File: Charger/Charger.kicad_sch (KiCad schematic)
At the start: 2 parts, among them J1 Charger output, SW1 Charger_Switch

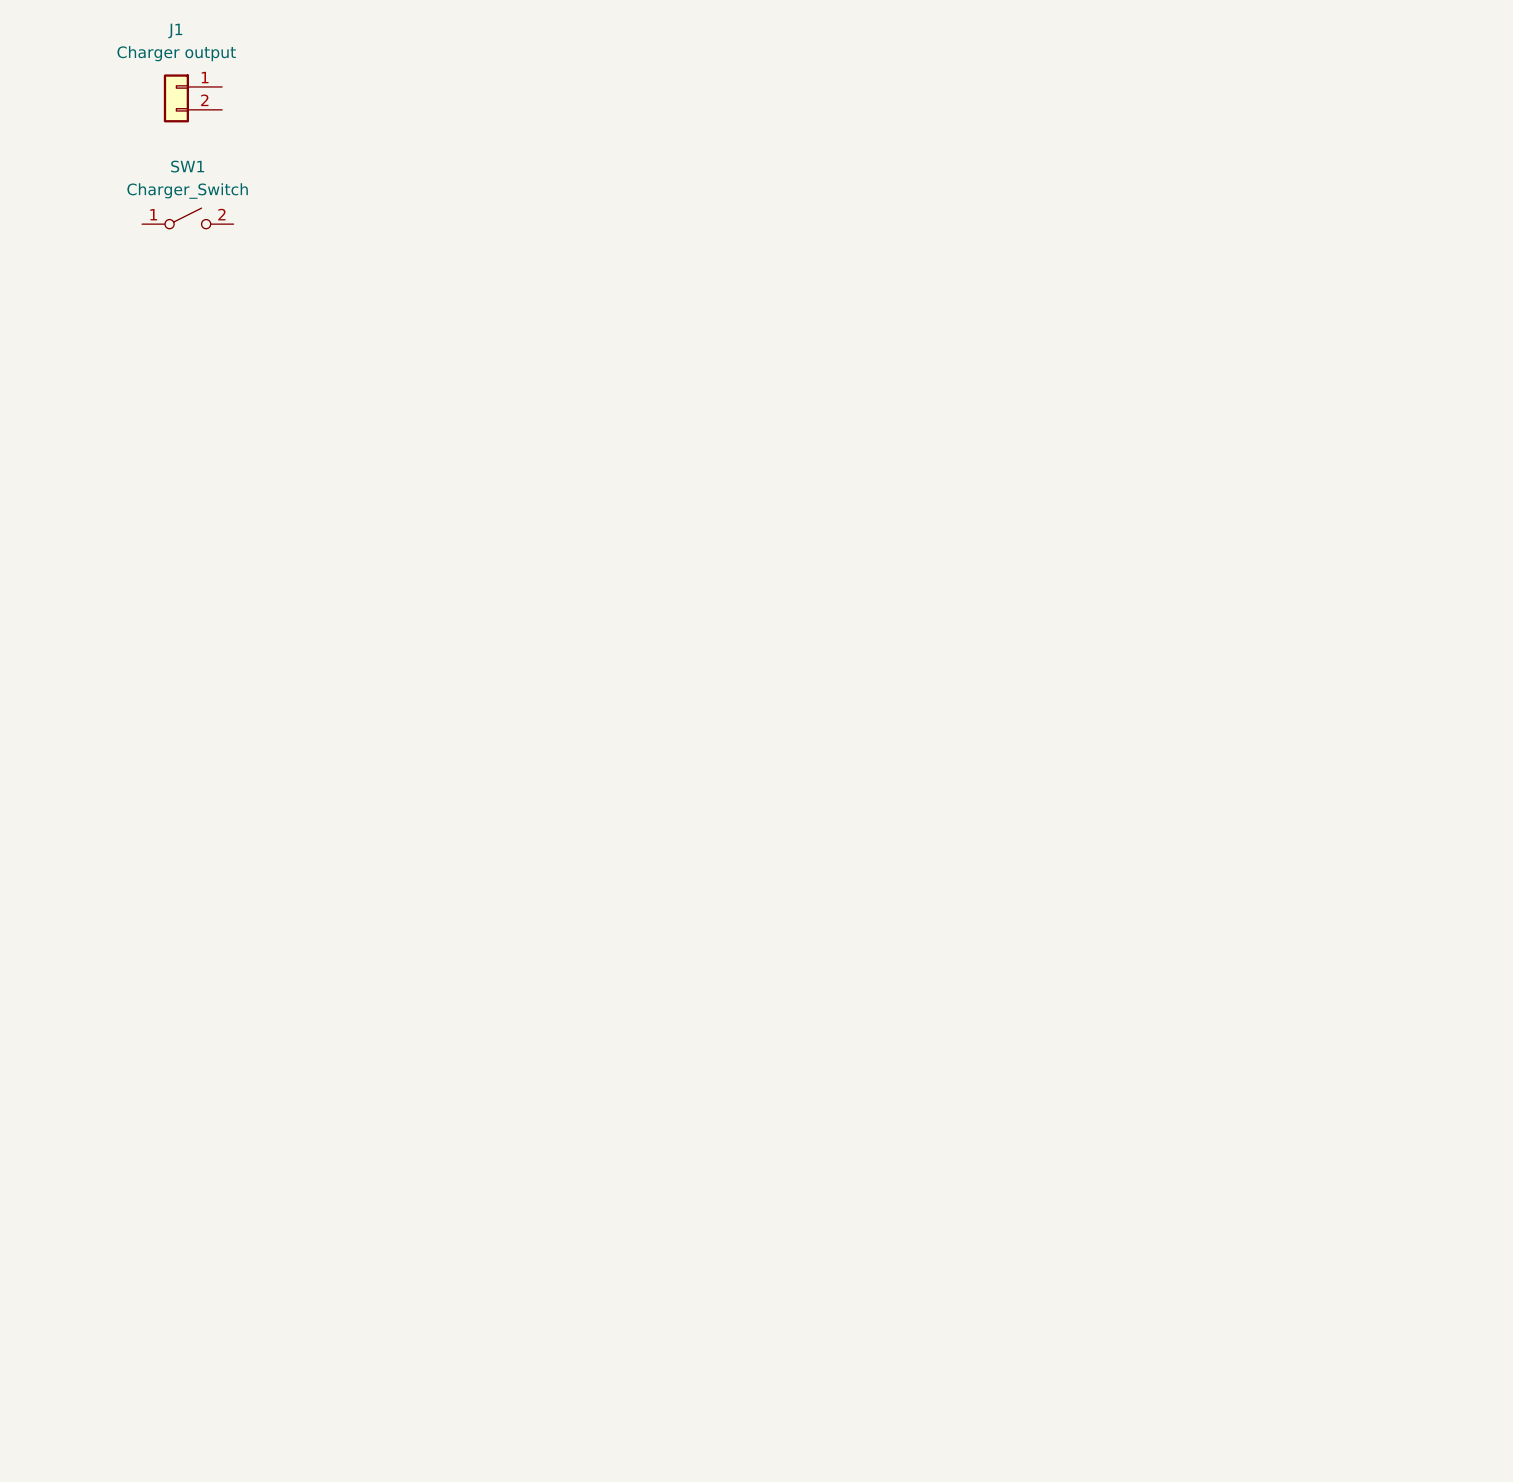
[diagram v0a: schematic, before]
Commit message: dot car charger
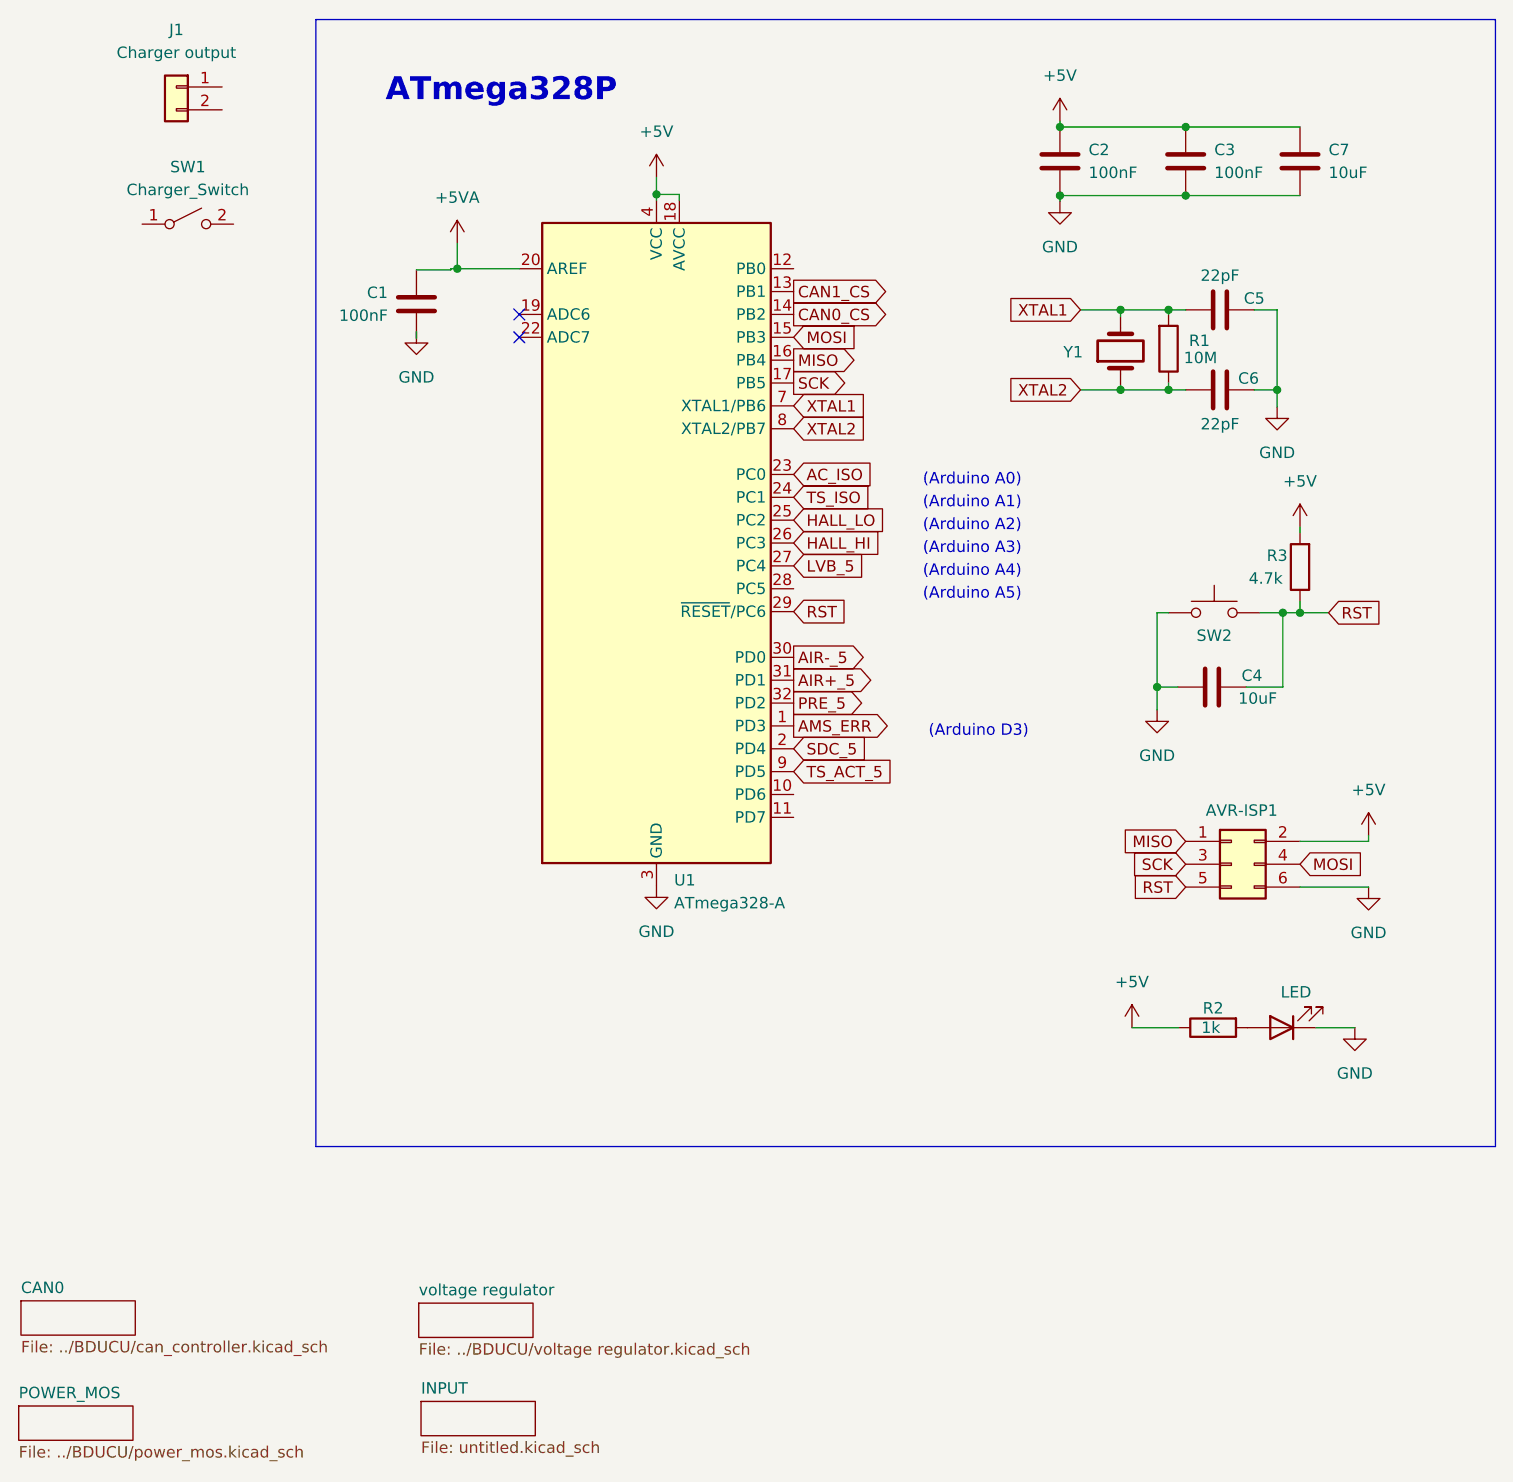
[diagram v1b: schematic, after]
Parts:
- added AVR-ISP1: Conn_02x03_Odd_Even, Connector_PinHeader_2.54mm:PinHeader_2x03_P2.54mm_Vertical, symbol Connector_Generic:Conn_02x03_Odd_Even
- added C1, C2, C3: 100nF, RMC_Capacitor:C_0805_2012Metric_Pad1.18x1.45mm_HandSolder_L, symbol Device:C
- added C4, C7: 10uF, RMC_Capacitor:C_0805_2012Metric_Pad1.18x1.45mm_HandSolder_L, symbol Device:C
- added C5, C6: 22pF, RMC_Capacitor:C_0805_2012Metric_Pad1.18x1.45mm_HandSolder_L, symbol Device:C
- added D1: LED, RMC_LED:LED_0805_2012Metric_Pad1.45x1.40mm_HandSolder, symbol Device:LED
- added R1: 10M, RMC_Resistor:R_0805_2012Metric_Pad1.20x1.40mm_HandSolder_L, symbol Device:R
- added R2: 1k, RMC_Resistor:R_0805_2012Metric_Pad1.20x1.40mm_HandSolder_L, symbol Device:R
- added R3: 4.7k, RMC_Resistor:R_0805_2012Metric_Pad1.20x1.40mm_HandSolder_L, symbol Device:R
- added SW2: SW_Push, Button_Switch_SMD:SW_SPST_CK_RS282G05A3, symbol Switch:SW_Push
- added U1: ATmega328-A, RMC_QFP:TQFP-32_7x7mm_P0.8mm_L, symbol MCU_Microchip_ATmega:ATmega328-A
- added Y1: 20MHz, RMC_Crystal:Crystal_HC49-U_Vertical_W_SMD, symbol Device:Crystal
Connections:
- new net: D1.2 (A), R2.2
- new net +5V: AVR-ISP1.2 (Pin_2), C2.2, C3.2, C7.2, R2.1, R3.2, U1.18 (AVCC), U1.4 (VCC), U1.6 (VCC)
- new net +5VA: C1.2, U1.20 (AREF)
- new net AC_ISO: U1.23 (PC0)
- new net AIR+_5: U1.31 (PD1)
- new net AIR-_5: U1.30 (PD0)
- new net AMS_ERR: U1.1 (PD3)
- new net CAN0_CS: U1.14 (PB2)
- new net CAN1_CS: U1.13 (PB1)
- new net GND: AVR-ISP1.6 (Pin_6), C1.1, C2.1, C3.1, C4.1, C5.1, C6.1, C7.1, D1.1 (K), SW2.1, U1.21 (GND), U1.3 (GND), U1.5 (GND)
- new net HALL_HI: U1.26 (PC3)
- new net HALL_LO: U1.25 (PC2)
- new net LVB_5: U1.27 (PC4)
- new net MISO: AVR-ISP1.1 (Pin_1), U1.16 (PB4)
- new net MOSI: AVR-ISP1.4 (Pin_4), U1.15 (PB3)
- new net PRE_5: U1.32 (PD2)
- new net RST: AVR-ISP1.5 (Pin_5), C4.2, R3.1, SW2.2, U1.29 (~{RESET}/PC6)
- new net SCK: AVR-ISP1.3 (Pin_3), U1.17 (PB5)
- new net SDC_5: U1.2 (PD4)
- new net TS_ACT_5: U1.9 (PD5)
- new net TS_ISO: U1.24 (PC1)
- new net XTAL1: C5.2, R1.2, U1.7 (XTAL1/PB6), Y1.2
- new net XTAL2: C6.2, R1.1, U1.8 (XTAL2/PB7), Y1.1
- no-connect marks 0 -> 2
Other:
- added sheet CAN0 (../BDUCU/can_controller.kicad_sch)
- added sheet INPUT (untitled.kicad_sch)
- added sheet POWER_MOS (../BDUCU/power_mos.kicad_sch)
- added sheet voltage regulator (../BDUCU/voltage regulator.kicad_sch)
- note added: "(Arduino A0)"
- note added: "(Arduino A1)"
- note added: "(Arduino A2)"
- note added: "(Arduino A3)"
- note added: "(Arduino A4)"
- note added: "(Arduino A5)"
- note added: "(Arduino D3)"
- note added: "ATmega328P"

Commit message: CHARGER
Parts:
- removed J1: Charger output, symbol Connector_Generic:Conn_01x02
- removed SW1: Charger_Switch, symbol Switch:SW_SPST
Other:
- added sheet Connectors (connectors.kicad_sch)
- added sheet DIGIPOT (DIGIPOT.kicad_sch)
- sheet CAN0 ports: added CAN_H, CAN_L, CS, MISO, MOSI, SCK; removed none
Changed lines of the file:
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@@
-	)
-	(symbol
-		(lib_id "Connector_Generic:Conn_01x02")
-		(at 38.1 38.1 0)
-		(mirror y)
-		(unit 1)
-		(exclude_from_sim no)
-		(in_bom yes)
-		(on_board yes)
-		(dnp no)
-		(fields_autoplaced yes)
-		(property "Reference" "J1"
-			(at 38.1 31.75 0)
-			(effects
-				(font
-					(size 1.27 1.27)
-				)
-			)
-		)
-		(property "Value" "Charger output"
-			(at 38.1 34.29 0)
-			(effects
-				(font
-					(size 1.27 1.27)
-				)
-			)
-		)
-		(property "Footprint" ""
-			(at 38.1 38.1 0)
-			(effects
-				(font
-					(size 1.27 1.27)
-				)
-				(hide yes)
-			)
-		)
-		(property "Datasheet" "~"
-			(at 38.1 38.1 0)
-			(effects
-				(font
-					(size 1.27 1.27)
-				)
-				(hide yes)
-			)
-		)
-		(property "Description" "Generic connector, single row, 01x02, script generated (kicad-library-utils/schlib/autogen/connector/)"
-			(at 38.1 38.1 0)
-			(effects
-				(font
-					(size 1.27 1.27)
-				)
-				(hide yes)
-			)
-		)
-		(pin "2"
-		)
-		(pin "1"
-		)
-		(instances
-			(project ""
-				(path "/ba218c5d-b6ee-4635-9cf5-de406e83bbdf"
-					(reference "J1")
-					(unit 1)
-				)
-			)
-		)
 	)
 	(symbol
@@
 	)
 	(symbol
-		(lib_id "Switch:SW_SPST")
-		(at 39.37 53.34 0)
-		(unit 1)
-		(exclude_from_sim no)
-		(in_bom yes)
-		(on_board yes)
-		(dnp no)
-		(fields_autoplaced yes)
-		(property "Reference" "SW1"
-			(at 39.37 46.99 0)
-			(effects
-				(font
-					(size 1.27 1.27)
-				)
-			)
-		)
-		(property "Value" "Charger_Switch"
-			(at 39.37 49.53 0)
-			(effects
-				(font
-					(size 1.27 1.27)
-				)
-			)
-		)
-		(property "Footprint" ""
-			(at 39.37 53.34 0)
-			(effects
-				(font
-					(size 1.27 1.27)
-				)
-				(hide yes)
-			)
-		)
-		(property "Datasheet" "~"
-			(at 39.37 53.34 0)
-			(effects
-				(font
-					(size 1.27 1.27)
-				)
-				(hide yes)
-			)
-		)
-		(property "Description" "Single Pole Single Throw (SPST) switch"
-			(at 39.37 53.34 0)
-			(effects
-				(font
-					(size 1.27 1.27)
-				)
-				(hide yes)
-			)
-		)
-		(pin "2"
-		)
-		(pin "1"
-		)
-		(instances
-			(project ""
-				(path "/ba218c5d-b6ee-4635-9cf5-de406e83bbdf"
-					(reference "SW1")
-					(unit 1)
-				)
-			)
-		)
-	)
-	(symbol
 		(lib_id "Device:R")
 		(at 162.941 91.44 180)
@@
 	)
 	(sheet
-		(at 65.278 184.15)
+		(at 20.955 156.845)
 		(size 12.7 3.81)
 		(exclude_from_sim no)
@@
 			(color 0 0 0 0.0000)
 		)
+		(property "Sheetname" "Connectors"
+			(at 20.955 156.1334 0)
+			(effects
+				(font
+					(size 1.27 1.27)
+				)
+				(justify left bottom)
+			)
+		)
+		(property "Sheetfile" "connectors.kicad_sch"
+			(at 20.955 161.2396 0)
+			(effects
+				(font
+					(size 1.27 1.27)
+				)
+				(justify left top)
+			)
+		)
+		(property "Field2" ""
+			(at 20.955 156.845 0)
+			(effects
+				(font
+					(size 1.27 1.27)
+				)
+			)
+		)
+		(instances
+			(project "Charger"
+				(path "/ba218c5d-b6ee-4635-9cf5-de406e83bbdf"
+					(page "6")
+				)
+			)
+		)
+	)
+	(sheet
+		(at 65.278 184.15)
+		(size 12.7 3.81)
+		(exclude_from_sim no)
+		(in_bom yes)
+		(on_board yes)
+		(dnp no)
+		(fields_autoplaced yes)
+		(stroke
+			(width 0.1524)
+			(type solid)
+		)
+		(fill
+			(color 0 0 0 0.0000)
+		)
 		(property "Sheetname" "INPUT"
 			(at 65.278 183.4384 0)
@@
 	)
 	(sheet
-		(at 20.828 172.974)
+		(at 113.03 173.99)
 		(size 12.7 3.81)
 		(exclude_from_sim no)
@@
 			(color 0 0 0 0.0000)
 		)
+		(property "Sheetname" "DIGIPOT"
+			(at 113.03 173.2784 0)
+			(effects
+				(font
+					(size 1.27 1.27)
+				)
+				(justify left bottom)
+			)
+		)
+		(property "Sheetfile" "DIGIPOT.kicad_sch"
+			(at 113.03 178.3846 0)
+			(effects
+				(font
+					(size 1.27 1.27)
+				)
+				(justify left top)
+			)
+		)
+		(instances
+			(project "Charger"
+				(path "/ba218c5d-b6ee-4635-9cf5-de406e83bbdf"
+					(page "7")
+				)
+			)
+		)
+	)
+	(sheet
+		(at 20.828 166.624)
+		(size 14.097 11.811)
+		(exclude_from_sim no)
+		(in_bom yes)
+		(on_board yes)
+		(dnp no)
+		(fields_autoplaced yes)
+		(stroke
+			(width 0.1524)
+			(type solid)
+		)
+		(fill
+			(color 0 0 0 0.0000)
+		)
 		(property "Sheetname" "CAN0"
-			(at 20.828 172.2624 0)
+			(at 20.828 165.9124 0)
 			(effects
 				(font
@@
 		)
 		(property "Sheetfile" "../BDUCU/can_controller.kicad_sch"
-			(at 20.828 177.3686 0)
+			(at 20.828 179.0196 0)
 			(effects
 				(font
@@
 			)
 		)
+		(pin "CAN_H" input
+			(at 34.925 171.45 0)
+			(effects
+				(font
+					(size 1.27 1.27)
+				)
+				(justify right)
+			)
+		)
+		(pin "CS" input
+			(at 20.828 176.53 180)
+			(effects
+				(font
+					(size 1.27 1.27)
+				)
+				(justify left)
+			)
+		)
+		(pin "MISO" input
+			(at 20.828 168.91 180)
+			(effects
+				(font
+					(size 1.27 1.27)
+				)
+				(justify left)
+			)
+		)
+		(pin "MOSI" input
+			(at 20.828 171.45 180)
+			(effects
+				(font
+					(size 1.27 1.27)
+				)
+				(justify left)
+			)
+		)
+		(pin "SCK" input
+			(at 20.828 173.99 180)
+			(effects
+				(font
+					(size 1.27 1.27)
+				)
+				(justify left)
+			)
+		)
+		(pin "CAN_L" input
+			(at 34.925 173.99 0)
+			(effects
+				(font
+					(size 1.27 1.27)
+				)
+				(justify right)
+			)
+		)

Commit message: funny stuffs
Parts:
- added J1: PL00X-301-10M8, symbol Connector_Generic:Conn_01x03
- added J2: PL00Y-301-10M8, symbol Connector_Generic:Conn_01x03
- added K1: Gigavc PNC11BDA, symbol Relay:Relay_SPST-NC
- added R4: discharge resistor, symbol Device:R
- added SW1: Emergency Button, symbol Switch:SW_Push
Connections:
- net AMS_ERR: no longer U1.1 (PD3)
- net GND: now also K1.A1
- net AC_ISO: no longer names the net of U1.23 (PC0)
- net AIR+_5: no longer names the net of U1.31 (PD1)
- net AIR-_5: no longer names the net of U1.30 (PD0)
- net CAN1_CS: no longer names the net of U1.13 (PB1)
- net HALL_HI: no longer names the net of U1.26 (PC3)
- net HALL_LO: no longer names the net of U1.25 (PC2)
- net LVB_5: no longer names the net of U1.27 (PC4)
- net PRE_5: no longer names the net of U1.32 (PD2)
- net SDC_5: no longer names the net of U1.2 (PD4)
- net TS_ACT_5 renamed ENABLE_5V
- net TS_ISO: no longer names the net of U1.24 (PC1)
- new net: J1.2 (Pin_2), SW1.1
- new net: J1.3 (Pin_3), J2.2 (Pin_2)
- new net: K1.11, R4.2
- new net +12V: SW1.2
- new net CHARGER_ERR: U1.1 (PD3)
- new net SDC_IN: K1.A2
- new net SDC_OUT: J2.3 (Pin_3)
- new net TS+: J1.1 (Pin_1), R4.1
- new net TS-: J2.1 (Pin_1), K1.12
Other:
- moved on the sheet: AVR-ISP1, C1, C2, C3, C4, C5, C6, C7, R1, R2, R3, SW2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

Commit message: Charger WIP
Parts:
- added K2: EV200 HAANA, Relay_THT:Relay_DPST_Omron_G2RL-2A, symbol Relay:G2RL-2A
- added SW3: SW_Push, Button_Switch_SMD:SW_SPST_CK_RS282G05A3, symbol Switch:SW_Push
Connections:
- net +12V: now also K2.23, SW3.1
- net SDC_IN: now also K2.A2
- net ENABLE_5V: no longer names the net of U1.9 (PD5)
- new net CHARGING_ENABLE: SW3.2
- new net HV_ON: K2.A1
- new net HV_PSU_LIVE: K2.14
- new net HV_RELAY_AUX: K2.24
- new net LIVE: K2.13
- no-connect marks 2 -> 4
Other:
- sheet POWER_MOS renamed POWER_MOS0
- removed sheet INPUT
- added sheet Digital input (SRU.kicad_sch)
- added sheet POWER_MOS1 (../BDUCU/power_mos.kicad_sch)
- sheet DIGIPOT ports: added A1, A2, B1, B2, CS, MISO, MOSI, RDY, SCK, W1, W2; removed none
- sheet POWER_MOS0 ports: added GND, OUT, SIGNAL, VIN; removed none
- note added: "A control"
- note added: "Charger error"
- note added: "HV supply enable relay"
- note added: "INDICATORS TSALG AMS ERR IMD ERR CHARGER ERR"
- note added: "TBD"
- note added: "V control"
- note added: "charging button"

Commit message: charger WIP
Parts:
- added D1, D2, D3, D4, D5: LED, symbol Device:LED
- renumbered D1 to D6, R4 to R1, R1 to R2, R2 to R3, R3 to R4
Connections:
- net +12V: now also D5.2 (A)
- net AMS_ERR: now also D1.2 (A)
- net GND: now also D1.1 (K), D2.1 (K), D3.1 (K), D4.1 (K)
- net HV_ON: now also D5.1 (K)
- net IMD_ERR: now also D2.2 (A)
- net TSAL_G: now also D3.2 (A)
- net SDA: now reaches U1.27 (PC4)
- net SCL: now reaches U1.28 (PC5)
- net DIGIPOT_RDY: now reaches U1.32 (PD2)
- new net CHARGER_ERR_12V: D4.2 (A)
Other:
- sheet CAN0: file ../BDUCU/can_controller.kicad_sch -> can_controller.kicad_sch
- sheet POWER_MOS0: file ../BDUCU/power_mos.kicad_sch -> power_mos.kicad_sch
- sheet POWER_MOS1: file ../BDUCU/power_mos.kicad_sch -> power_mos.kicad_sch
- sheet voltage regulator: file ../BDUCU/voltage regulator.kicad_sch -> voltage regulator.kicad_sch
- note added: "HVPSU"
- note added: "HVPSU measurement PCB"
- note added: "I2C"
- note added: "J"
- note added: "LVPSU"
- note added: "SDC IN"
- note added: "TODO: test HVPSU precharge behaviour test HVPSU pot response curve IV measurement slave retrofit the HVPSU switch to be ring terminals"
- note added: "buttons and"
- note added: "charger PCB"
- note added: "charger measurement slave"
- note added: "charging enable button"
- note added: "hall sensor V measurement"
- note added: "indicator lights"
- note added: "junction box (only does inputs)"
- note added: "power line"
- note added: "relay digipots"
- note added: "screen"
- note added: "use extension cord for split into HVPSU and LVPSU"
- note removed: "Charger error"
- note removed: "HV supply enable relay"
- note removed: "charging button"
- moved on the sheet: SW3
